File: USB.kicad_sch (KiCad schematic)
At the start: 12 parts, among them J6 USB_C_Receptacle_USB2.0_16P, U12 FT234XD-R, U13 TPD4EUSB30

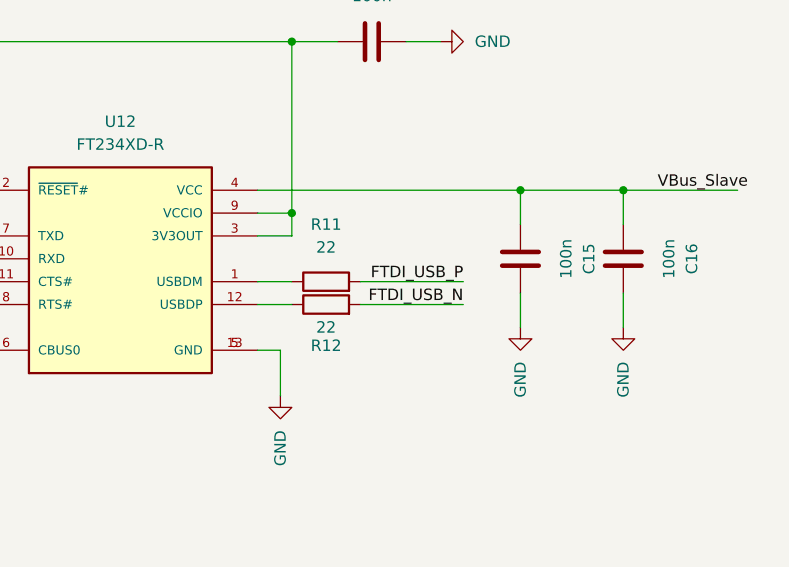
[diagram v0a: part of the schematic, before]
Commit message: fix: BOM issues and FTDI wiring (#2)
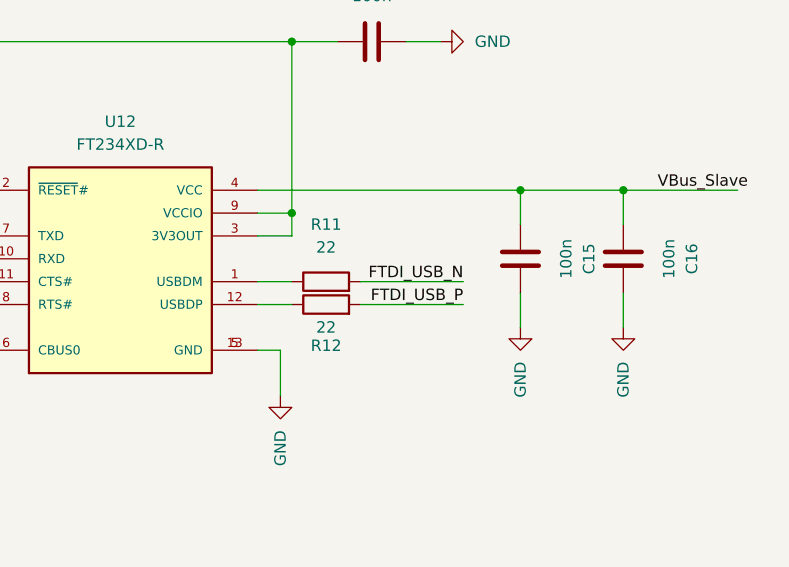
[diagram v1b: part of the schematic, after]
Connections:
- net FTDI_USB_N: now also R11.2; no longer R12.2
- net FTDI_USB_P: now also R12.2; no longer R11.2
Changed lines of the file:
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@@
 		)
 	)
-	(label "FTDI_USB_N"
+	(label "FTDI_USB_P"
 		(at 246.38 135.89 180)
 		(fields_autoplaced yes)
@@
 		)
 	)
-	(label "FTDI_USB_P"
+	(label "FTDI_USB_N"
 		(at 246.38 133.35 180)
 		(fields_autoplaced yes)

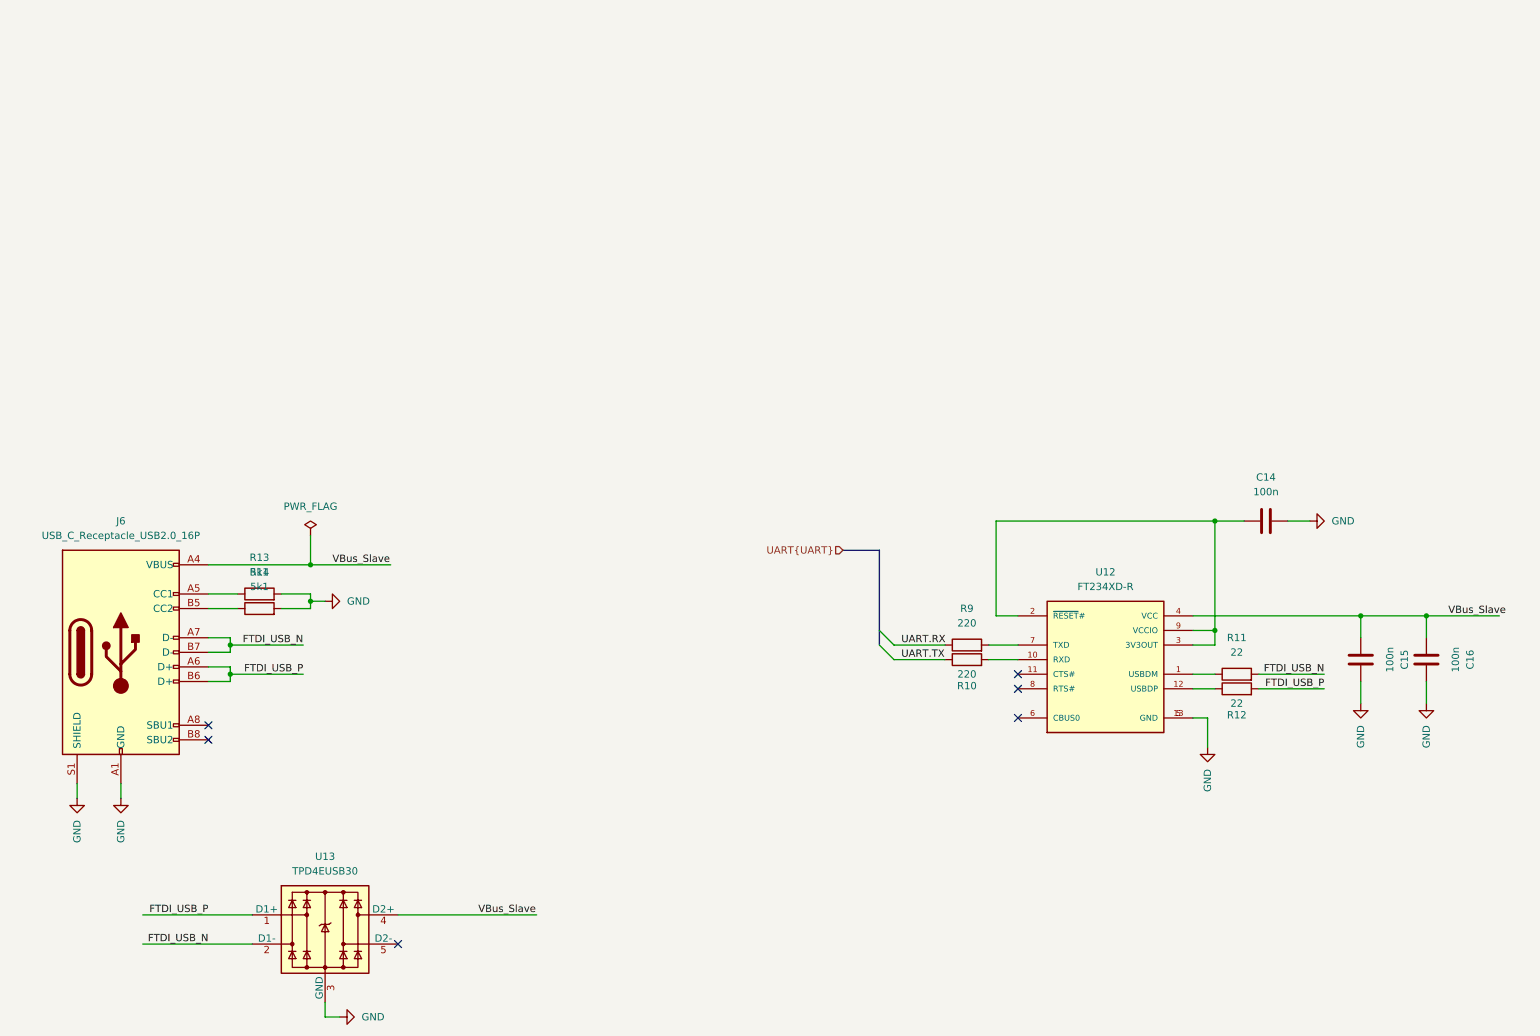
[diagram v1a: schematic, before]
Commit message: feat: switch UART chipset
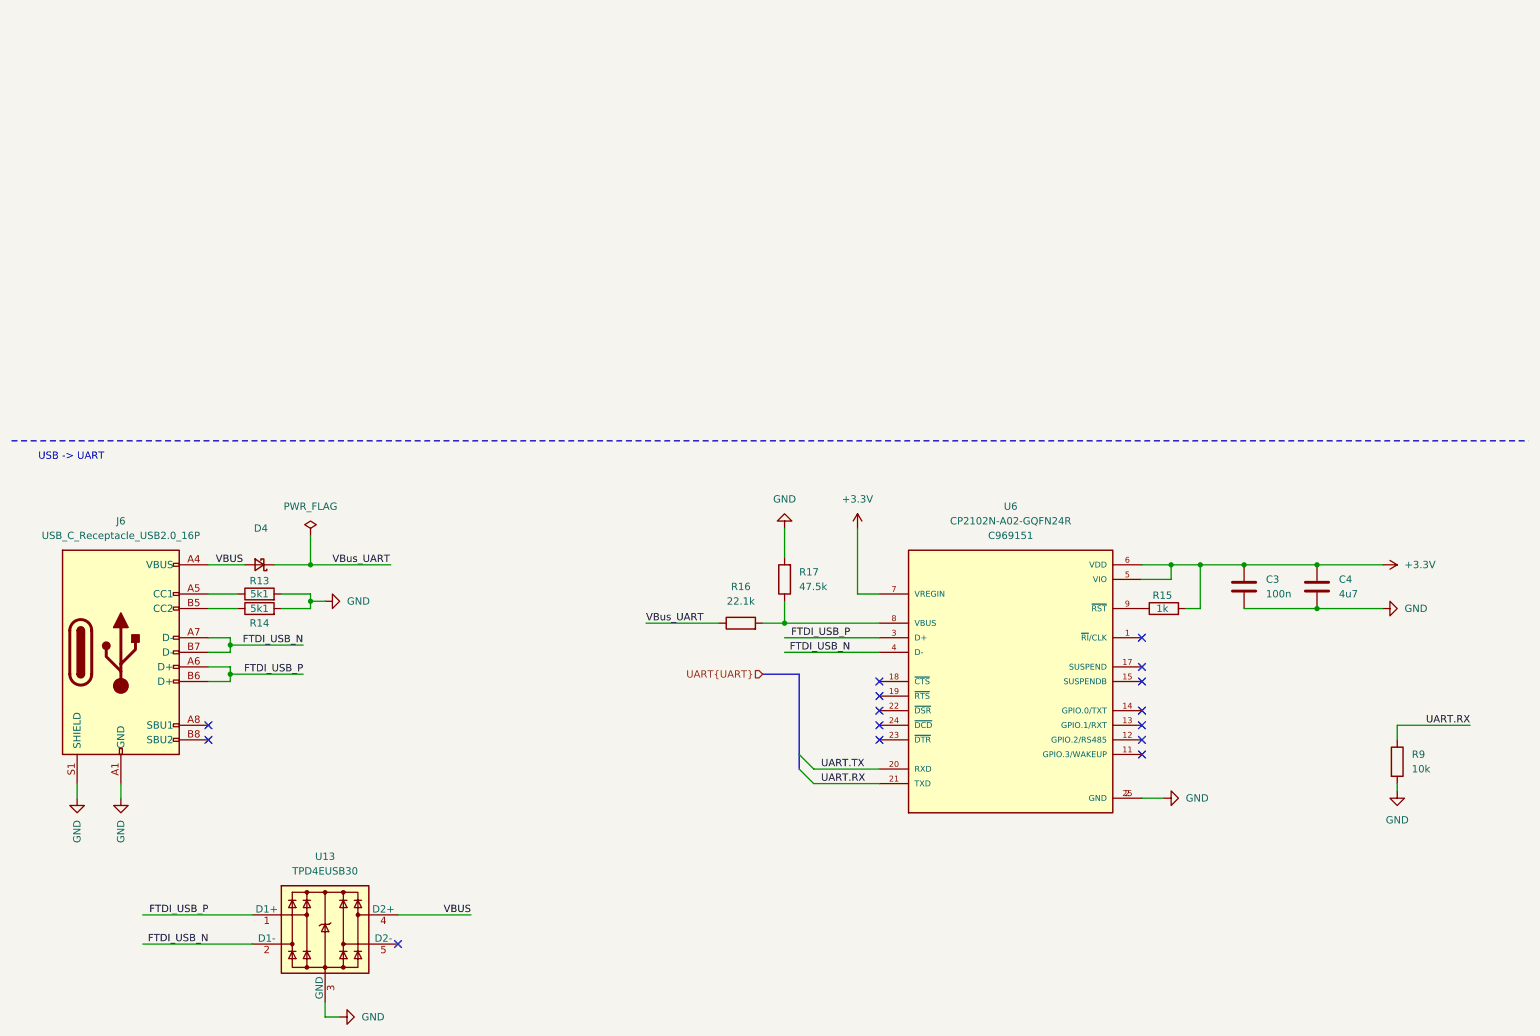
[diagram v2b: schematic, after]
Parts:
- removed C14, C15, C16: 100n, Capacitor_SMD:C_0402_1005Metric, symbol HomeLabIO:C
- removed R10: 220, Resistor_SMD:R_0402_1005Metric, symbol HomeLabIO:R
- removed R11, R12: 22, Resistor_SMD:R_0402_1005Metric, symbol HomeLabIO:R
- removed U12: FT234XD-R, HomeLabIO:SON45P300X300X80-13N, symbol HomeLabIO:FT234XD-R
- added C3: 100n, Capacitor_SMD:C_0402_1005Metric, symbol HomeLabIO:C
- added C4: 4u7, Capacitor_SMD:C_0402_1005Metric, symbol HomeLabIO:C
- added D4: D_Schottky_Small, Diode_SMD:D_0402_1005Metric, symbol Device:D_Schottky_Small
- added R15: 1k, Resistor_SMD:R_0402_1005Metric, symbol HomeLabIO:R
- added R16: 22.1k, Resistor_SMD:R_0402_1005Metric, symbol HomeLabIO:R
- added R17: 47.5k, Resistor_SMD:R_0402_1005Metric, symbol HomeLabIO:R
- added U6: CP2102N-A02-GQFN24R, HomeLabIO:QFN50P400X400X80-25N, symbol HomeLabIO:CP2102N-A02-GQFN24R
- R9: value 220 -> 10k; JLCPCB Part # C226351 -> C202396; MPN AC0402FR-07220RL -> CR0402-FX-1002GLF; Manufacturer YAGEO -> Bourns
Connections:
- net FTDI_USB_N: now also U6.4 (D-)
- net FTDI_USB_P: now also U6.3 (D+)
- net GND: now also R9.2, C3.1, C4.2, R17.2, U6.2 (GND), U6.25 (GND)
- net UART.RX: now also U6.21 (TXD)
- net UART.TX: now also U6.20 (RXD)
- net VBus_Slave renamed VBUS
- net VBUS: now also D4.2 (A)
- new net: R16.2, R17.1, U6.8 (VBUS)
- new net: R15.1, U6.9 (~{RST})
- new net +3.3V: C3.2, C4.1, R15.2, U6.5 (VIO), U6.6 (VDD), U6.7 (VREGIN)
- new net VBus_UART: D4.1 (K), R16.1
- no-connect marks 6 -> 15
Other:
- note added: "USB -> UART"

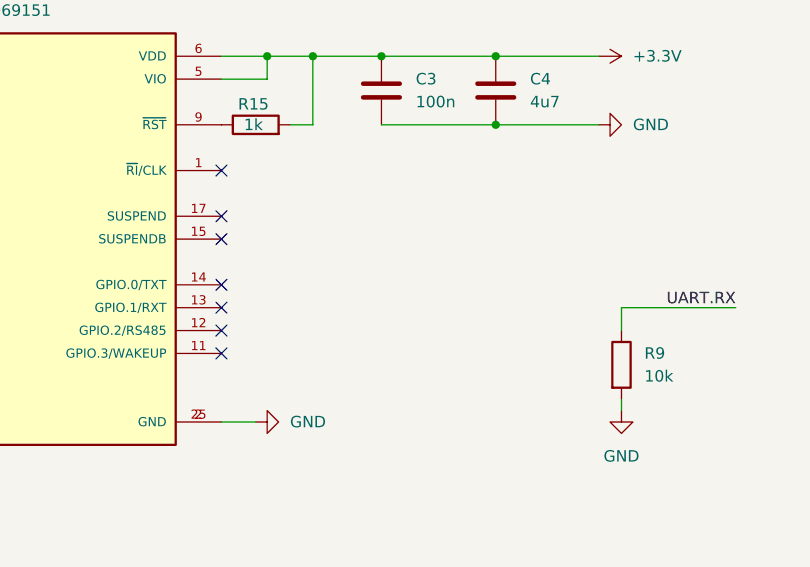
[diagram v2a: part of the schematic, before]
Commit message: feat: add UART activity LEDs (#7)
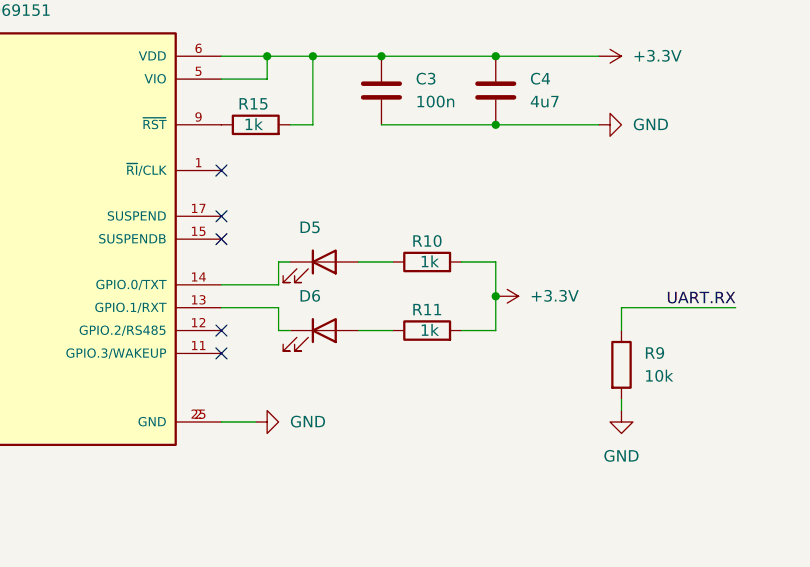
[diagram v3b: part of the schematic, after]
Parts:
- added D5, D6: LED, LED_SMD:LED_0603_1608Metric, symbol HomeLabIO:LED
- added R10, R11: 1k, Resistor_SMD:R_0402_1005Metric, symbol HomeLabIO:R
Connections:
- net +3.3V: now also R10.2, R11.2
- net at U6.13 (GPIO.1/RXT): now also D6.1 (K)
- net at U6.14 (GPIO.0/TXT): now also D5.1 (K)
- new net: D5.2 (A), R10.1
- new net: D6.2 (A), R11.1
- no-connect marks 15 -> 13

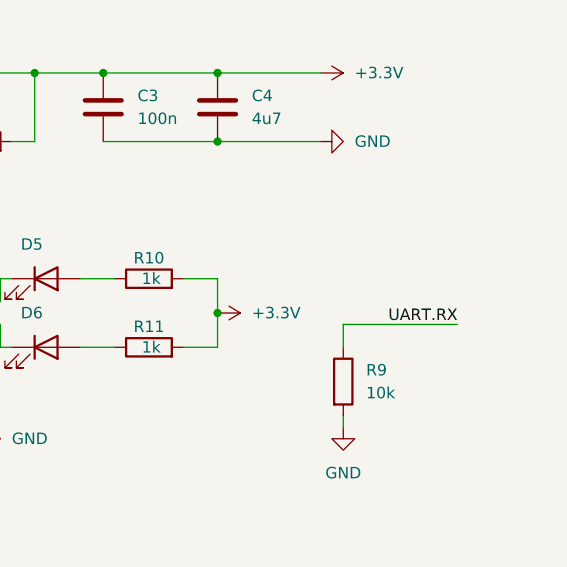
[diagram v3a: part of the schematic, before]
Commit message: fix: minor issues (#20)
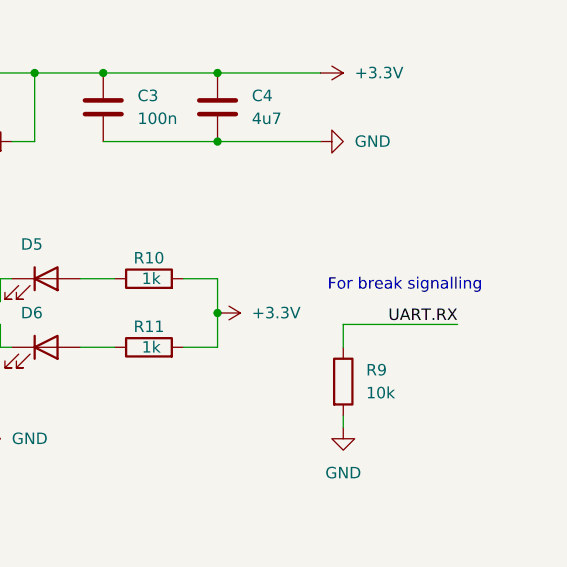
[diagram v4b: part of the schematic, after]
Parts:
- D4: MPN CDBQR0130L-HF -> CDBQR0130L-HF
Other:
- note added: "For break signalling"
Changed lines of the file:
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@@
+		)
+	)
+	(text "For break signalling"
+		(exclude_from_sim no)
+		(at 265.938 137.922 0)
+		(effects
+			(font
+				(size 1.27 1.27)
+			)
 		)
 	)
@@
 			)
 		)
-		(property "MPN" " CDBQR0130L-HF"
+		(property "MPN" "CDBQR0130L-HF"
 			(at 60.96 114.3 0)
 			(effects

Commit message: feat: TPM and GPIO (#22)
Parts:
- C3: footprint Capacitor_SMD:C_0402_1005Metric -> Hardware Components:C_0402_1005Metric; symbol HomeLabIO:C -> Hardware Components:C_100n_0402_16V
- C4: footprint Capacitor_SMD:C_0402_1005Metric -> Hardware Components:C_0402_1005Metric; symbol HomeLabIO:C -> Hardware Components:C_4u7_0402_16V
- D4: footprint Diode_SMD:D_0402_1005Metric -> Hardware Components:D_0402_1005Metric; symbol Device:D_Schottky_Small -> Hardware Components:D_0402_30V_100mA; JLCPCB Part # C2886014 -> C2886012; MPN CDBQR0130L-HF -> CDBQC0130L-HF
- D5: footprint LED_SMD:LED_0603_1608Metric -> Hardware Components:LED_0603_1608Metric; symbol HomeLabIO:LED -> Hardware Components:LED_O_0603_LTST-C191KFKT; MPN LTST-C191KFKT -> LTST-C191KFKT
- D6: footprint LED_SMD:LED_0603_1608Metric -> Hardware Components:LED_0603_1608Metric; symbol HomeLabIO:LED -> Hardware Components:LED_O_0603_LTST-C191KFKT
- J6: footprint Connector_USB:USB_C_Receptacle_HRO_TYPE-C-31-M-12 -> Hardware Components:USB_C_Receptacle_XUNPU_TYPEC-305-ACP16H458; symbol Connector:USB_C_Receptacle_USB2.0_16P -> Hardware Components:USB_C_Receptacle_XUNPU_TYPEC-305-ACP16H458; JLCPCB Part # C165948 -> C5454943; MPN TYPE-C-31-M-12 -> TYPEC-305-ACP16H458; Manufacturer Korean Hroparts Elec -> XUNPU
- R10, R11, R15: footprint Resistor_SMD:R_0402_1005Metric -> Hardware Components:R_0402_1005Metric; symbol HomeLabIO:R -> Hardware Components:R_1k_0402_75V
- R13, R14: footprint Resistor_SMD:R_0402_1005Metric -> Hardware Components:R_0402_1005Metric; symbol HomeLabIO:R -> Hardware Components:R_5k1_0402_50V
- R16: value 22.1k -> 22k1; footprint Resistor_SMD:R_0402_1005Metric -> Hardware Components:R_0402_1005Metric; symbol HomeLabIO:R -> Hardware Components:R_22k1_0402_50V
- R17: value 47.5k -> 47k5; footprint Resistor_SMD:R_0402_1005Metric -> Hardware Components:R_0402_1005Metric; symbol HomeLabIO:R -> Hardware Components:R_47k5_0402_50V
- R9: footprint Resistor_SMD:R_0402_1005Metric -> Hardware Components:R_0402_1005Metric; symbol HomeLabIO:R -> Hardware Components:R_10k_0402_50V
- U13: footprint Package_SON:USON-10_2.5x1.0mm_P0.5mm -> Hardware Components:TPD4EUSB30_USON-10; symbol HomeLabIO:TPD4EUSB30 -> Hardware Components:ESD_TPD4EUSB30
- U6: footprint HomeLabIO:QFN50P400X400X80-25N -> Hardware Components:CP2102-A02-GQ-QFN-50P; symbol HomeLabIO:CP2102N-A02-GQFN24R -> Hardware Components:CP2102-A02-GQ
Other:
- title: (none) -> HomeLabIO
- moved on the sheet: C3, C4, D4, D5, D6, R10, R11, R13, R14, R15, R16, R17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
